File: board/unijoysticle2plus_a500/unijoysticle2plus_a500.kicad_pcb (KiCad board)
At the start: 4 copper layers, 67 x 52 mm, 47 parts, among them J1 USB_B_Micro, J2 PORT JOY #1, J3 PORT JOY #2, Q1 S8050, Q2 S8050, SW1 RESET, SW2 BOOT, SW3 USER1, SW4 USER2, U1 ESP32-WROOM-32E, U2 AMS1117-3.3, U3 CH340C, U4 74HC05, U5 74HC05, U6 74HC05

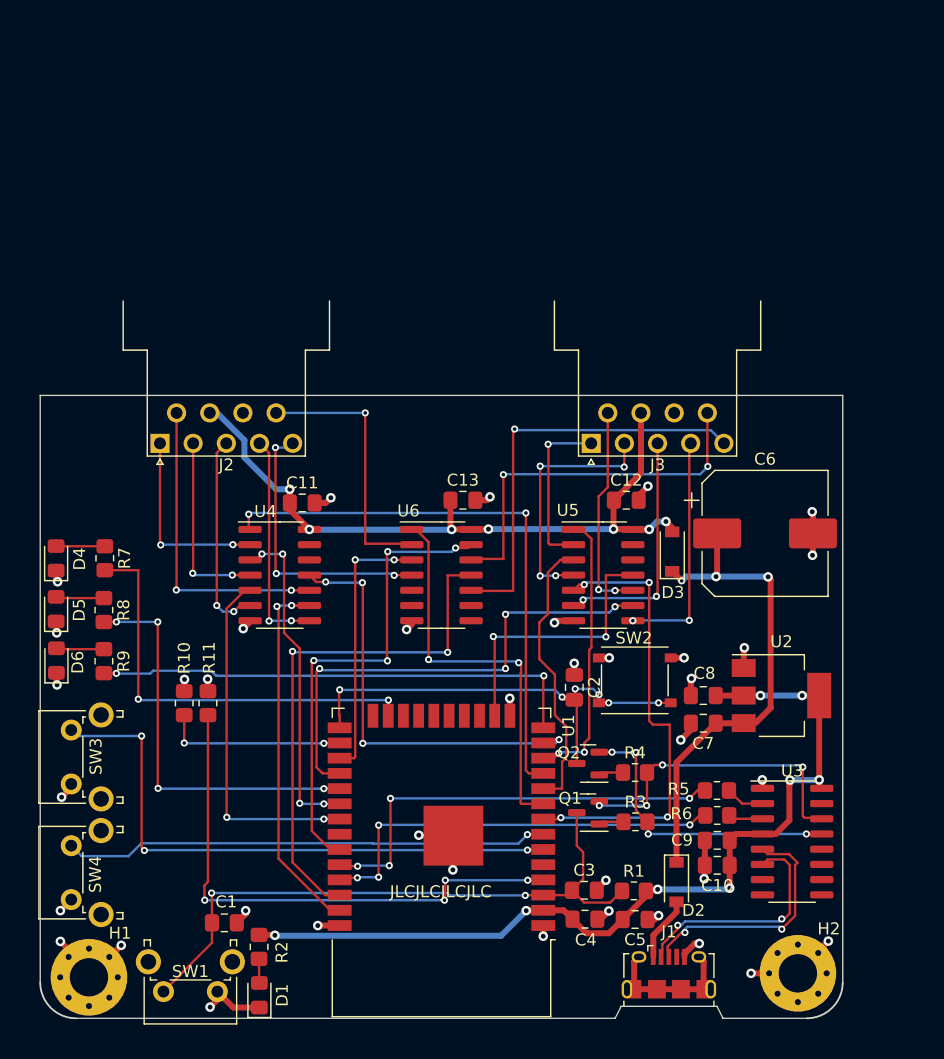
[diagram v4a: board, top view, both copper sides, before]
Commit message: Uni 2+ A500: many little changes
- replace resistor 0 with solder jumper for strapping pins
- move big cap a big down
- improved routing
- move vias outside pads
... and more
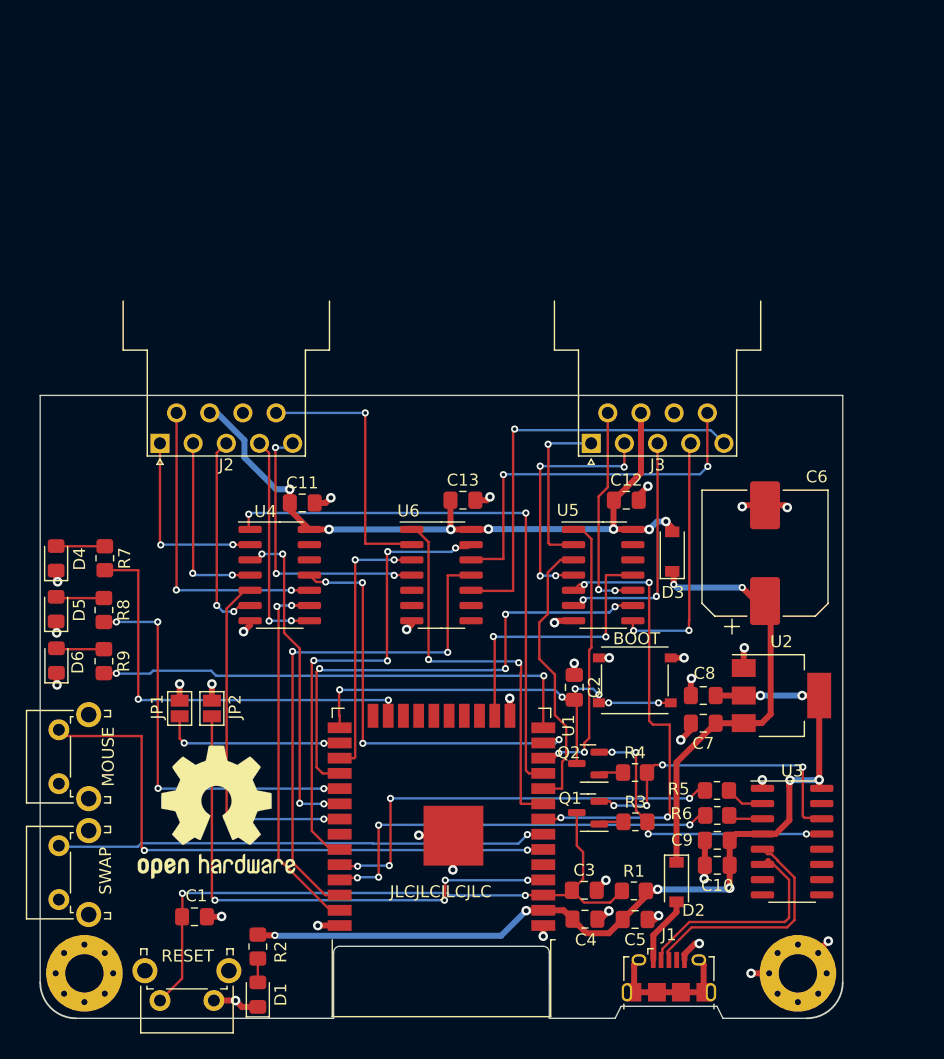
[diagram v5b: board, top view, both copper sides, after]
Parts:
- removed R10, R11: 0, Resistor_SMD:R_0805_2012Metric_Pad1.20x1.40mm_HandSolder
- added G***: LOGO, Unijoysticle:unijoysticle_logo, B.Cu at (113.7, 114.1)
- added JP1: SolderJumper_2_Open, Jumper:SolderJumper-2_P1.3mm_Open_Pad1.0x1.5mm, F.Cu at (91.6, 122.1)
- added JP2: SolderJumper_2_Open, Jumper:SolderJumper-2_P1.3mm_Open_Pad1.0x1.5mm, F.Cu at (94.3, 122.1)
- added REF**: OSHW-Logo2_14.6x12mm_SilkScreen, Symbol:OSHW-Logo2_14.6x12mm_SilkScreen, F.Cu at (94.7, 130.8)
- SW3: value USER1 -> MOUSE
- SW4: value USER2 -> SWAP
- moved C1 2.54 mm to (92.9, 139.5)
- moved C6 1.65 mm to (140.5, 109.2), turned to 90 degrees
- moved SW3 1.03 mm to (81.6, 128.4)
- moved SW4 1.03 mm to (81.6, 138.1)
- moved SW1 0.80 mm to (94.5, 146.5)
- moved H1 0.50 mm to (83.7, 144.2)
- moved J1 0.25 mm to (132.5, 144.5)
- moved D1 0.14 mm to (98.2, 146.0)
- moved R2 0.10 mm to (98.2, 142.0)
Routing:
- net GND: track 66.7 -> 55.4 mm, vias 38 -> 34
- net Net-(C6-Pad1): track 40.3 -> 36.8 mm, vias 3 -> 2
- net /ESP32/ESP_EN: track 52.4 -> 54.6 mm
- net /Amiga Ports/J2_RIGHT: track 19.6 -> 21.2 mm
- net /USB Serial & Power/USBD+: track 20.9 -> 19.6 mm, vias 2 -> 0
- net GPIO_SWITCH_USER1: track 49.0 -> 50.1 mm, vias 3 -> 2
- net GPIO_BOOTSTRAP_36: track 45.5 -> 44.5 mm
- net /USB Serial & Power/USBD-: track 19.7 -> 18.9 mm, vias 2 -> 0
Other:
- outline, holes or cut-outs redrawn
- board text added: "Unijoysticle️ 2+ A500 Rev. A"
- board text removed: "Unijoysticle 2+ A500 Rev. A"

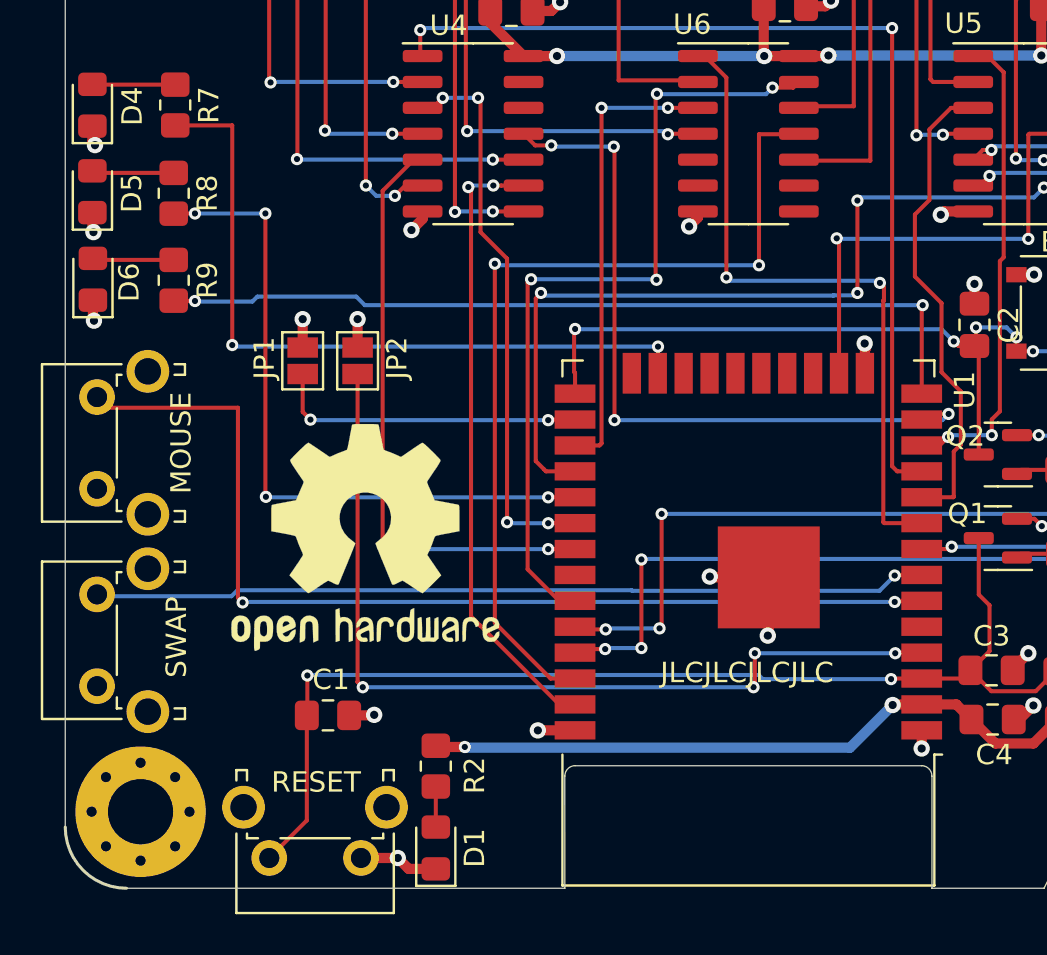
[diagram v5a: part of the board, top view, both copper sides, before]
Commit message: A500: Reuse GPIO 15 both as LED and BoardId
Cannot use GPIOs 34~39 for Board ID since in previous models those leds
were floating and those GPIOs don't have pull-up/pull-down resistors.

To GPIO 15 is reused for board id and LEDs.

GPIO 36 and 39 and grounded for future-compatibility.

FIXME:Push buttons won't work. They require a pull-up/pull-down
resistor.
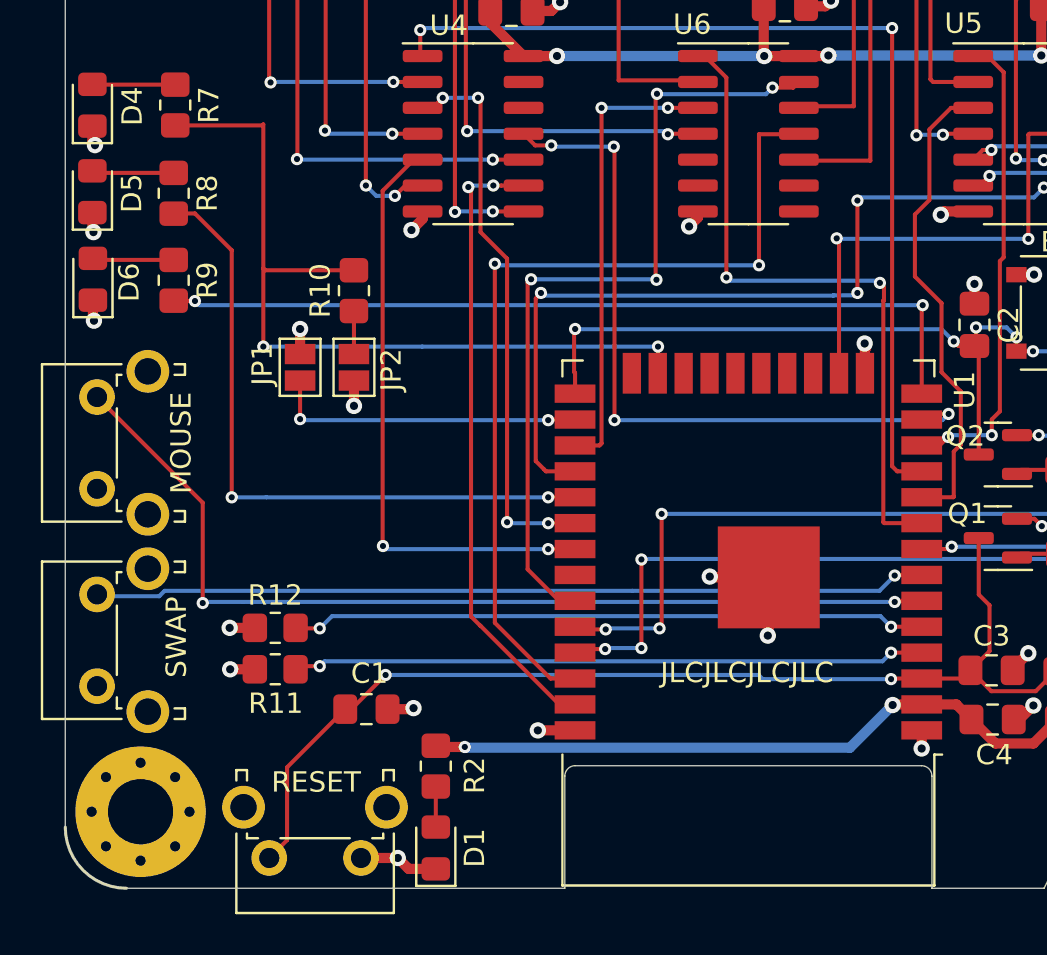
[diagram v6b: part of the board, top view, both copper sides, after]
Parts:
- removed REF**: OSHW-Logo2_14.6x12mm_SilkScreen, Symbol:OSHW-Logo2_14.6x12mm_SilkScreen
- added R10: 1K, Resistor_SMD:R_0805_2012Metric_Pad1.20x1.40mm_HandSolder, F.Cu at (94.2, 118.7)
- added R11: 0, Resistor_SMD:R_0805_2012Metric_Pad1.20x1.40mm_HandSolder, F.Cu at (90.3, 137.3)
- added R12: 0, Resistor_SMD:R_0805_2012Metric_Pad1.20x1.40mm_HandSolder, F.Cu at (90.3, 135.2)
- JP1: value SolderJumper_2_Open -> SolderJumper_1_Open
- moved C1 1.91 mm to (94.8, 139.2)
- moved JP2 0.37 mm to (94.2, 122.5), turned to 90 degrees
- moved JP1 0.34 mm to (91.5, 122.5)
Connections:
- net GPIO_LED_BT renamed GPIO_BOOTSTRAP_15_LED_BT
- JP2 pad 2: GPIO_BOOTSTRAP_36 -> Net-(JP2-Pad2)
- U1 pad 4: GPIO_BOOTSTRAP_36 -> GPIO_36
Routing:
- net GPIO_BOOTSTRAP_36: track 44.5 -> 0.00 mm, vias 4 -> 0
- net GPIO_39: track 0.00 -> 31.2 mm, vias 0 -> 2
- net GPIO_36: track 0.00 -> 31.0 mm, vias 0 -> 2
- net GPIO_BOOTSTRAP_15_LED_BT: track 35.8 -> 40.4 mm
- net GPIO_SWITCH_USER1: track 50.1 -> 47.6 mm
- net GND: track 55.4 -> 57.6 mm, vias 34 -> 36
- net Net-(JP2-Pad2): track 0.00 -> 2.11 mm
- net /ESP32/ESP_EN: track 54.6 -> 52.6 mm
- net GPIO_LED_J1: track 33.6 -> 32.5 mm, vias 4 -> 2

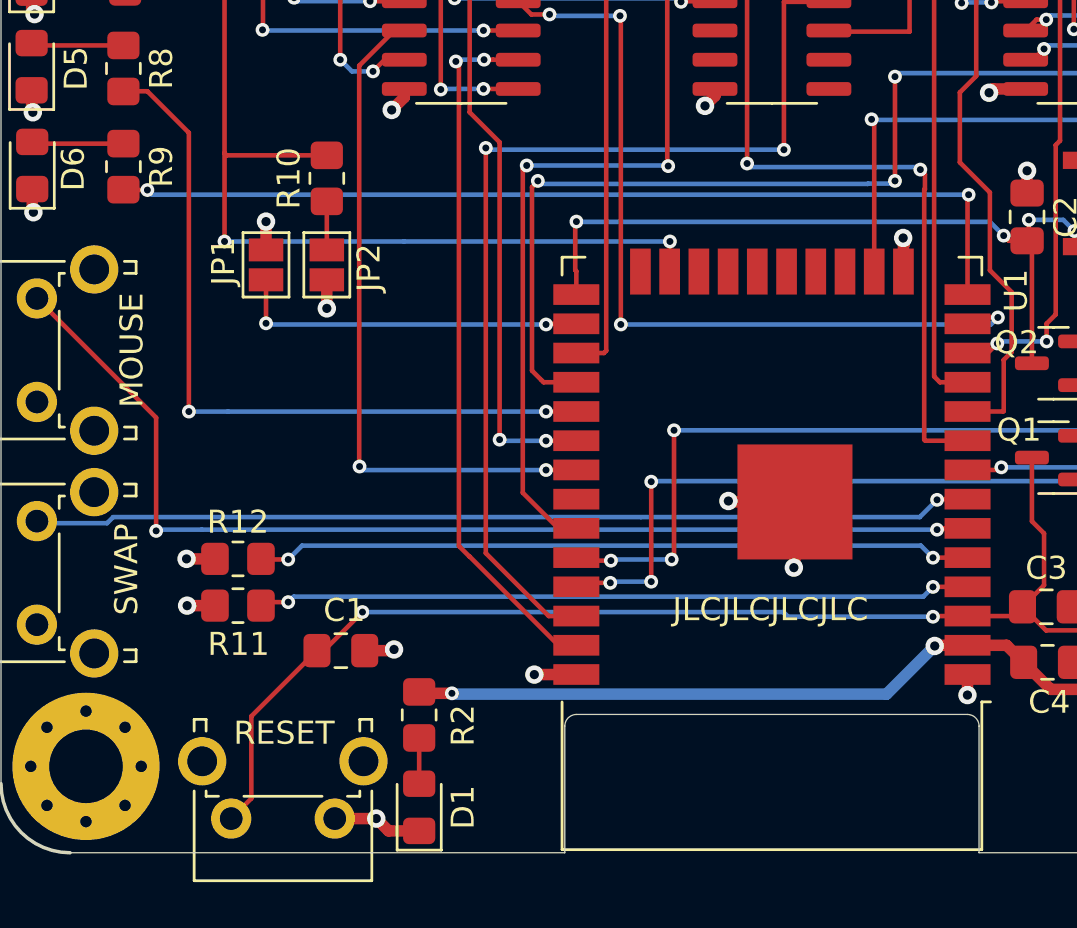
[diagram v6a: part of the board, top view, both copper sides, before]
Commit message: a500: add pull-up resistor to push buttons
GPIOs 34~39 don't have internal pull-up.
Add external ones
a#	modified:   unijoysticle2plus_a500.kicad_sch
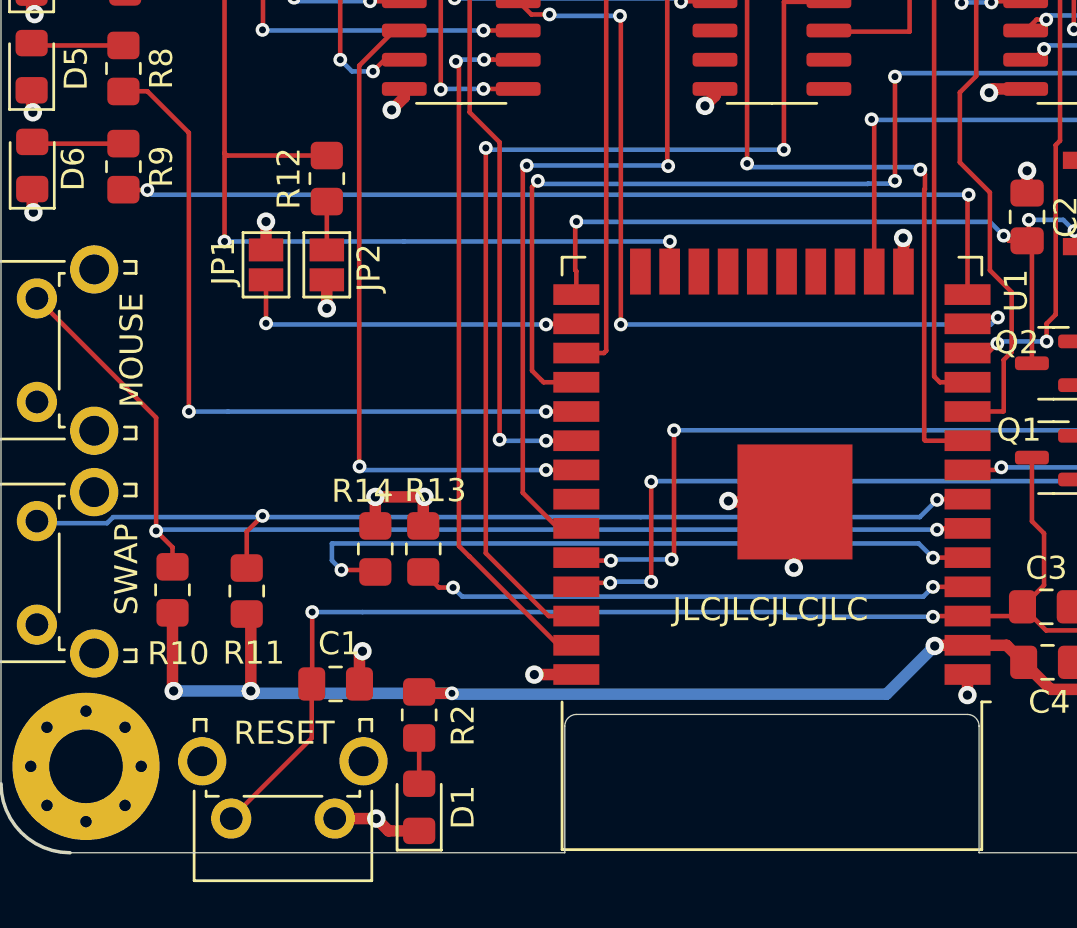
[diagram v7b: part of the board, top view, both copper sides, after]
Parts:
- added R13: 0, Resistor_SMD:R_0805_2012Metric_Pad1.20x1.40mm_HandSolder, F.Cu at (98.3, 134.8)
- added R14: 0, Resistor_SMD:R_0805_2012Metric_Pad1.20x1.40mm_HandSolder, F.Cu at (96.3, 134.8)
- R10: value 1K -> 10K
- R11: value 0 -> 10K
- R12: value 0 -> 1K
- moved R10 19.1 mm to (87.5, 136.6)
- moved R12 17.0 mm to (94.2, 118.7), turned to 90 degrees
- moved C1 1.47 mm to (94.5, 140.7)
- moved R11 0.74 mm to (90.7, 136.6), turned to 90 degrees
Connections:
- R10 pad 1: Net-(JP2-Pad2) -> +3V3
- R10 pad 2: GPIO_BOOTSTRAP_15_LED_BT -> GPIO_SWITCH_USER1
- R11 pad 1: GND -> +3V3
- R11 pad 2: GPIO_36 -> GPIO_SWITCH_USER2
- R12 pad 1: GND -> Net-(JP2-Pad2)
- R12 pad 2: GPIO_39 -> GPIO_BOOTSTRAP_15_LED_BT
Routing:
- net +3V3: track 74.9 -> 93.9 mm, vias 8 -> 10
- net GPIO_36: track 31.0 -> 24.3 mm
- net GPIO_SWITCH_USER2: track 40.9 -> 43.5 mm, vias 1 -> 2
- net GND: track 57.6 -> 60.0 mm
- net GPIO_SWITCH_USER1: track 47.6 -> 49.4 mm
- net /ESP32/ESP_EN: track 52.6 -> 53.7 mm

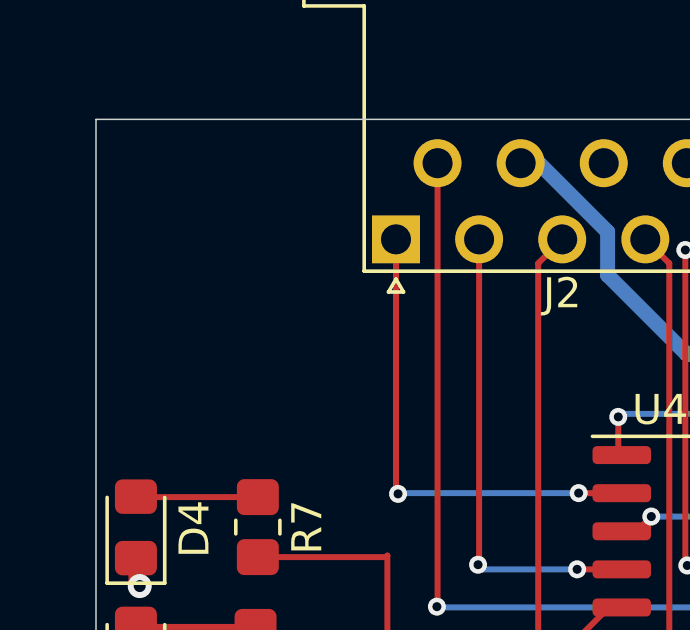
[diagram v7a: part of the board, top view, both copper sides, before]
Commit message: Rename Uni2+ A500 to Uni2 A500
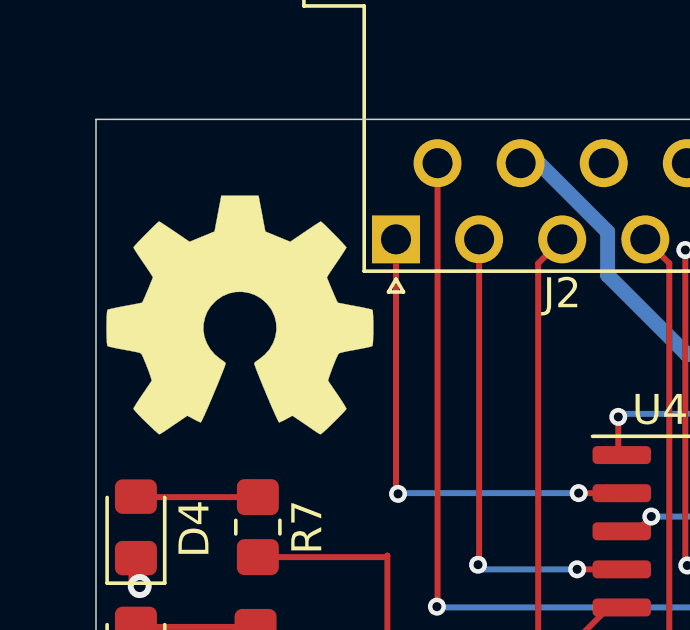
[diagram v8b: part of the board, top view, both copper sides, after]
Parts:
- added REF**: OSHW-Symbol_8.9x8mm_SilkScreen, Symbol:OSHW-Symbol_8.9x8mm_SilkScreen, F.Cu at (84.8, 102.5)
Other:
- board text added: "Unijoysticle 2 A500 Rev. A"
- board text removed: "Unijoysticle️ 2+ A500 Rev. A"
